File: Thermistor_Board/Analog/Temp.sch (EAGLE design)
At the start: 39 parts, among them J1 IO, J2 SJ-3523-SMT-TR, J3 SJ-3523-SMT-TR, J5 SJ-3523-SMT-TR

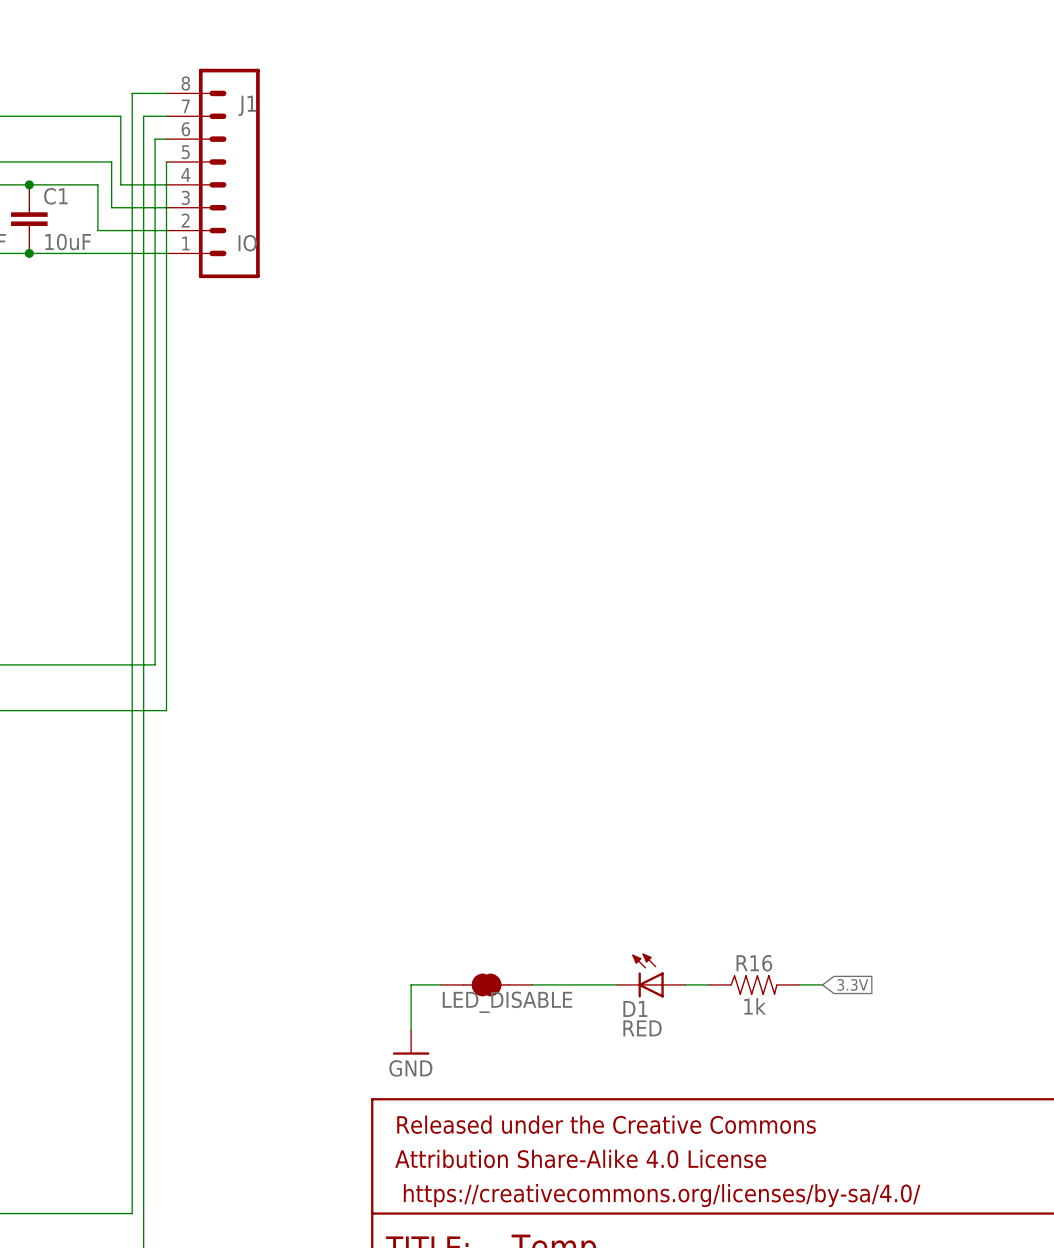
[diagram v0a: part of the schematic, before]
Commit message: Board Updates
All LEDs at same location
Separated analog and digital ground
Updated impedance components
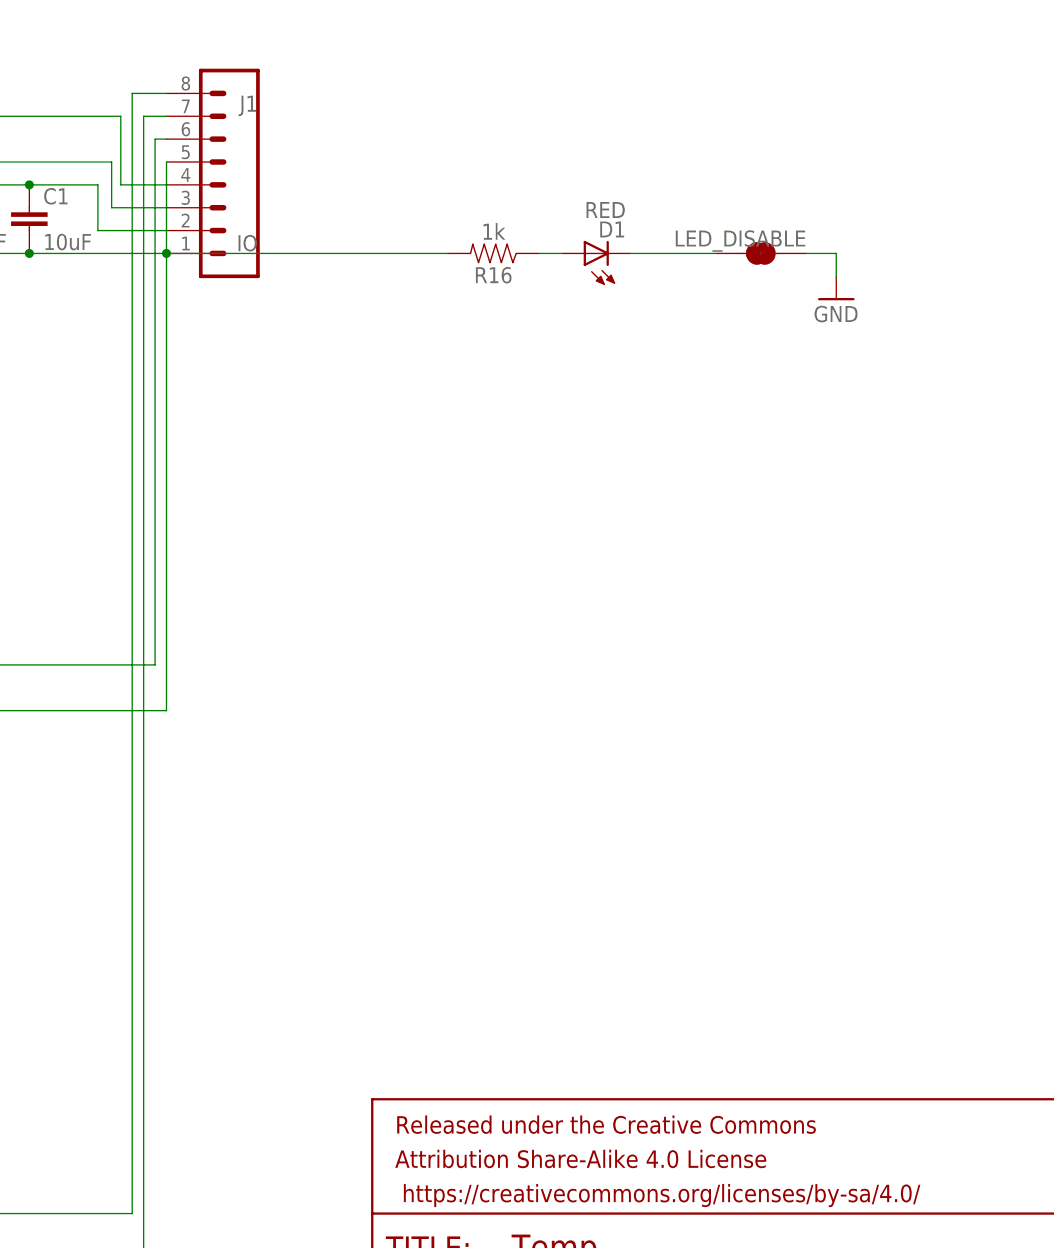
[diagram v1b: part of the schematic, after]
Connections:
- removed net N$12: J1.5, JP6.2
- net 3.3V: no longer R16.2
- net N$15: now also R16.2
- net N$16: now also J1.5, JP6.2
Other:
- moved on the sheet: D1, LED_DISABLE, R16
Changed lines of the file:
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@@
 <attribute name="VALUE" x="164.084" y="140.081" size="1.778" layer="96" font="vector"/>
 </instance>
-<instance part="R16" gate="G$1" x="253.238" y="58.42" smashed="yes">
-<attribute name="NAME" x="253.238" y="59.944" size="1.778" layer="95" font="vector" align="bottom-center"/>
-<attribute name="VALUE" x="253.238" y="56.896" size="1.778" layer="96" font="vector" align="top-center"/>
-</instance>
-<instance part="D1" gate="G$1" x="243.078" y="58.42" smashed="yes" rot="R270">
-<attribute name="NAME" x="238.506" y="54.864" size="1.778" layer="95"/>
-<attribute name="VALUE" x="238.506" y="52.705" size="1.778" layer="96"/>
-</instance>
-<instance part="GND4" gate="1" x="215.138" y="50.8" smashed="yes">
-<attribute name="VALUE" x="212.598" y="48.26" size="1.778" layer="96"/>
-</instance>
-<instance part="LED_DISABLE" gate="G$1" x="223.52" y="58.42" smashed="yes">
-<attribute name="NAME" x="218.44" y="55.88" size="1.778" layer="95" font="vector"/>
-<attribute name="VALUE" x="220.98" y="55.88" size="1.778" layer="96" font="vector" align="top-left" display="off"/>
+<instance part="R16" gate="G$1" x="224.282" y="139.7" smashed="yes" rot="R180">
+<attribute name="NAME" x="224.282" y="138.176" size="1.778" layer="95" font="vector" rot="R180" align="bottom-center"/>
+<attribute name="VALUE" x="224.282" y="141.224" size="1.778" layer="96" font="vector" rot="R180" align="top-center"/>
+</instance>
+<instance part="D1" gate="G$1" x="234.442" y="139.7" smashed="yes" rot="R90">
+<attribute name="NAME" x="239.014" y="143.256" size="1.778" layer="95" rot="R180"/>
+<attribute name="VALUE" x="239.014" y="145.415" size="1.778" layer="96" rot="R180"/>
+</instance>
+<instance part="GND4" gate="1" x="262.382" y="134.62" smashed="yes">
+<attribute name="VALUE" x="259.842" y="132.08" size="1.778" layer="96"/>
+</instance>
+<instance part="LED_DISABLE" gate="G$1" x="254" y="139.7" smashed="yes" rot="R180">
+<attribute name="NAME" x="259.08" y="142.24" size="1.778" layer="95" font="vector" rot="R180"/>
+<attribute name="VALUE" x="256.54" y="142.24" size="1.778" layer="96" font="vector" rot="R180" align="top-left" display="off"/>
 </instance>
 <instance part="FRAME1" gate="G$1" x="63.5" y="10.16" smashed="yes"/>
@@
 <segment>
 <pinref part="GND4" gate="1" pin="GND"/>
-<wire x1="215.138" y1="53.34" x2="215.138" y2="58.42" width="0.1524" layer="91"/>
+<wire x1="262.382" y1="137.16" x2="262.382" y2="139.7" width="0.1524" layer="91"/>
 <pinref part="LED_DISABLE" gate="G$1" pin="1"/>
-<wire x1="215.138" y1="58.42" x2="218.44" y2="58.42" width="0.1524" layer="91"/>
+<wire x1="262.382" y1="139.7" x2="259.08" y2="139.7" width="0.1524" layer="91"/>
 </segment>
 <segment>
@@
 <net name="3.3V" class="0">
 <segment>
-<wire x1="260.858" y1="58.42" x2="258.318" y2="58.42" width="0.1524" layer="91"/>
-<label x="260.858" y="58.42" size="1.27" layer="95" xref="yes"/>
-<pinref part="R16" gate="G$1" pin="2"/>
-</segment>
-<segment>
 <wire x1="124.46" y1="63.5" x2="124.46" y2="124.46" width="0.1524" layer="91"/>
 <pinref part="R2" gate="G$1" pin="1"/>
@@
 <pinref part="R16" gate="G$1" pin="1"/>
 <pinref part="D1" gate="G$1" pin="A"/>
-<wire x1="245.618" y1="58.42" x2="248.158" y2="58.42" width="0.1524" layer="91"/>
+<wire x1="231.902" y1="139.7" x2="229.362" y2="139.7" width="0.1524" layer="91"/>
 </segment>
 </net>
@@
 <segment>
 <pinref part="D1" gate="G$1" pin="C"/>
-<wire x1="237.998" y1="58.42" x2="228.6" y2="58.42" width="0.1524" layer="91"/>
+<wire x1="239.522" y1="139.7" x2="248.92" y2="139.7" width="0.1524" layer="91"/>
 <pinref part="LED_DISABLE" gate="G$1" pin="2"/>
 </segment>
@@
 </segment>
 </net>
-<net name="N$12" class="0">
-<segment>
-<pinref part="J1" gate="G$1" pin="5"/>
-<pinref part="JP6" gate="G$1" pin="2"/>
-<wire x1="187.96" y1="88.9" x2="187.96" y2="149.86" width="0.1524" layer="91"/>
-<wire x1="137.16" y1="88.9" x2="187.96" y2="88.9" width="0.1524" layer="91"/>
-</segment>
-</net>
 <net name="N$10" class="0">
 <segment>
@@
 <pinref part="JP4" gate="G$1" pin="2"/>
 <wire x1="137.16" y1="139.7" x2="162.56" y2="139.7" width="0.1524" layer="91"/>
+<wire x1="187.96" y1="139.7" x2="219.202" y2="139.7" width="0.1524" layer="91"/>
+<junction x="187.96" y="139.7"/>
+<pinref part="R16" gate="G$1" pin="2"/>
 </segment>
 </net>
@@
 <pinref part="JP3" gate="G$1" pin="2"/>
 <wire x1="137.16" y1="144.78" x2="139.7" y2="144.78" width="0.1524" layer="91"/>
-</segment>
-</net>
+<pinref part="J1" gate="G$1" pin="5"/>
+<pinref part="JP6" gate="G$1" pin="2"/>
+<wire x1="187.96" y1="88.9" x2="187.96" y2="142.24" width="0.1524" layer="91"/>
+<wire x1="187.96" y1="142.24" x2="187.96" y2="149.86" width="0.1524" layer="91"/>
+<wire x1="137.16" y1="88.9" x2="187.96" y2="88.9" width="0.1524" layer="91"/>
+</segment>
+</net>
